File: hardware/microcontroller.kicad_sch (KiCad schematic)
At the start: 12 parts, among them J1 AVR-ISP-6, SW2 SKRPACE010, U1 ATMEGA328P-AU, Y2 Crystal-32kHz

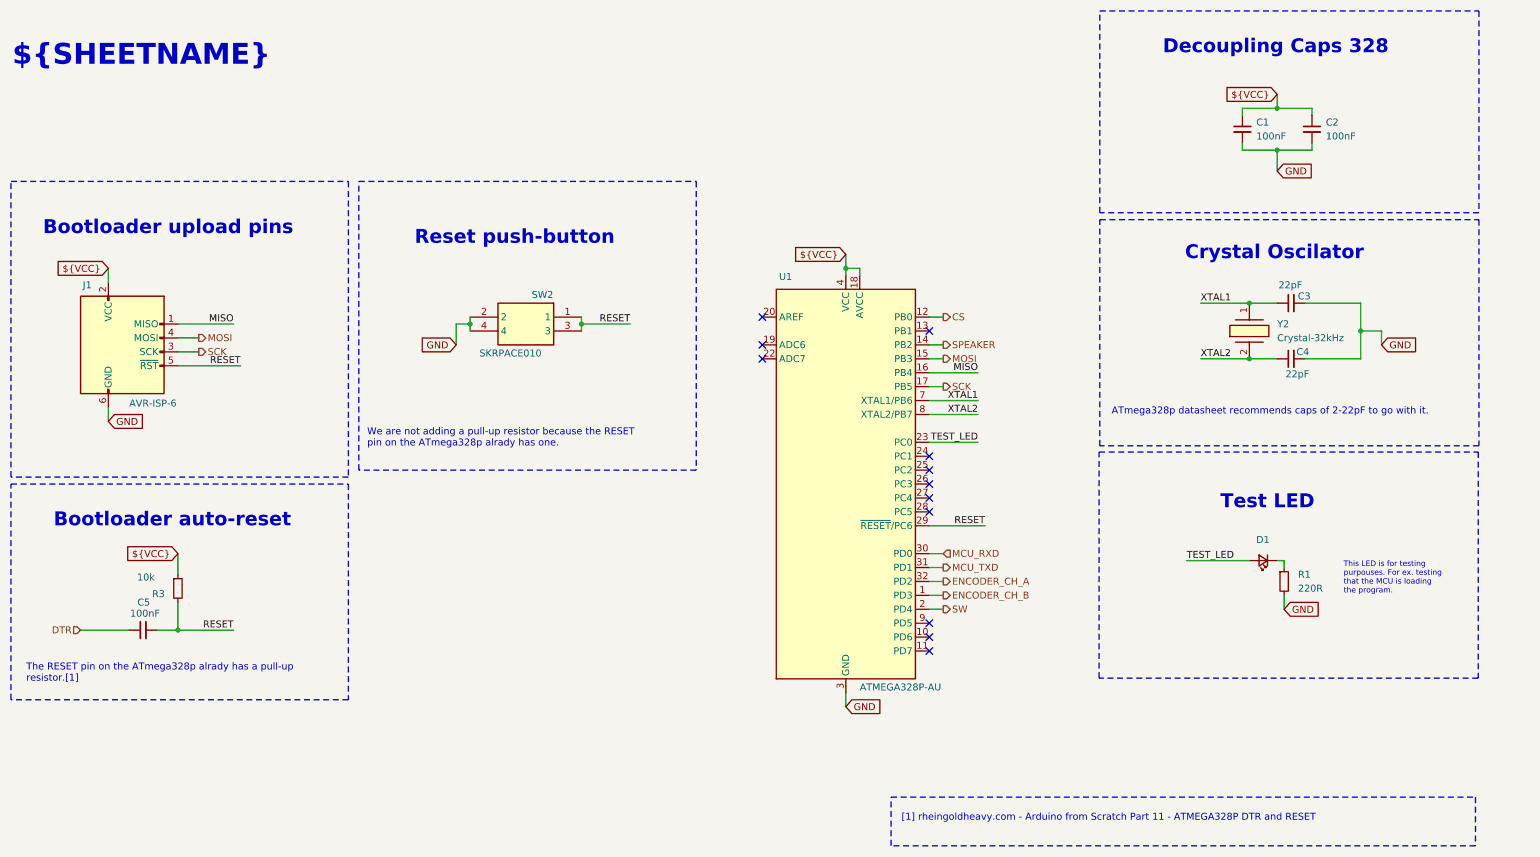
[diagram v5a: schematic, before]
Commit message: Symbols pins vs footprint pins checked
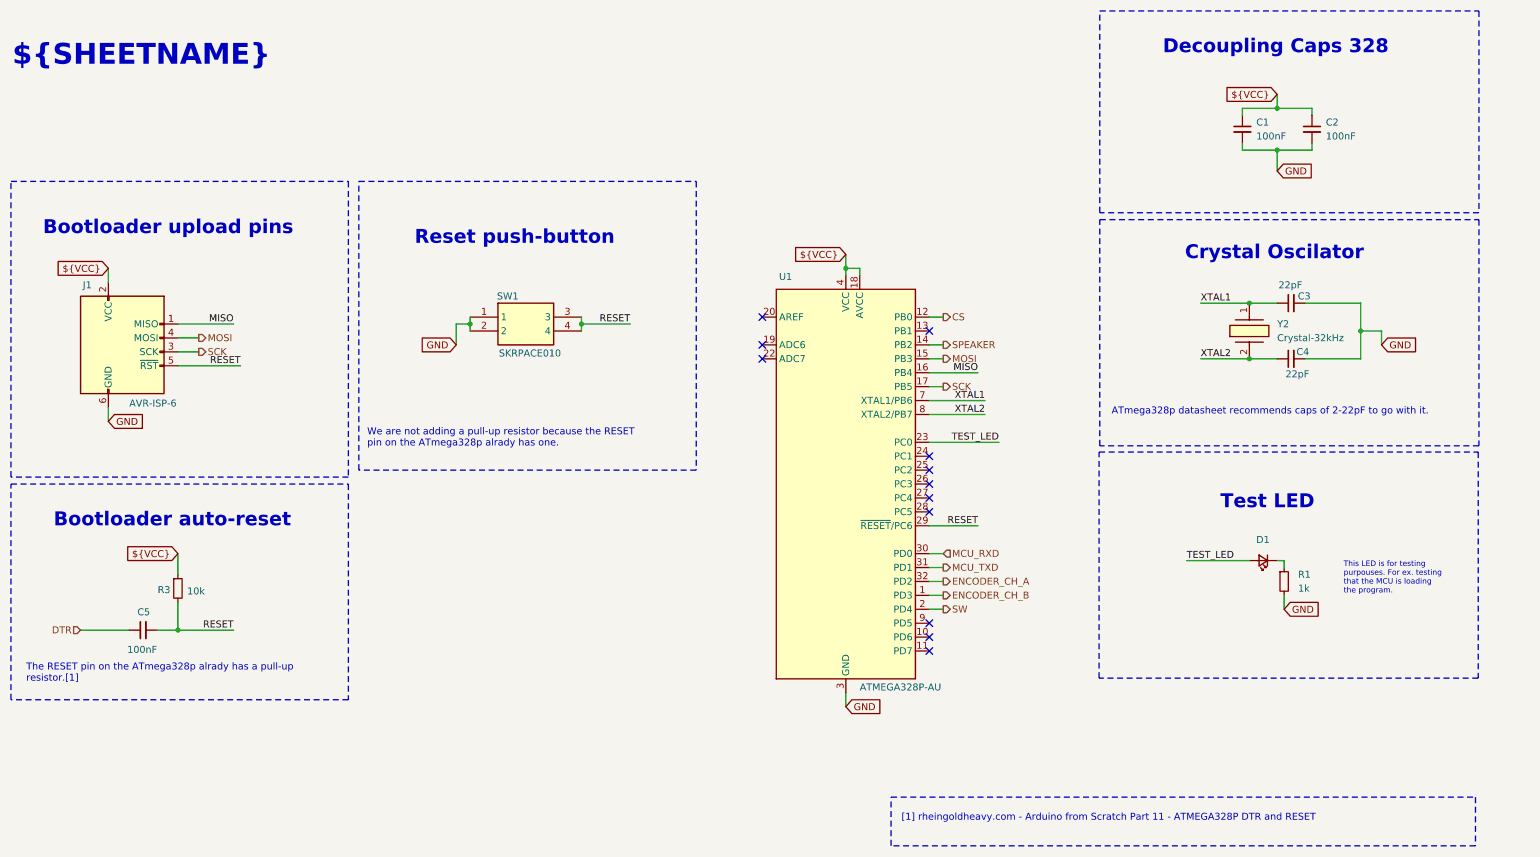
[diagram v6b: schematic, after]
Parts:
- removed SW2: SKRPACE010, kitchen_timer:SW_SKRPACE010, symbol kitchen_timer-symbols_lib:SKRPACE010
- added SW1: SKRPACE010, kitchen_timer:SW_SKRPACE010, symbol kitchen_timer-symbols_lib:SKRPACE010
- R1: value 220R -> 1k; footprint (none) -> Resistor_SMD:R_0805_2012Metric_Pad1.20x1.40mm_HandSolder; Manuf. Name (none) -> UNI-ROYAL(Uniroyal Elec); Manuf. Part # (none) -> 0805W8F1001T5E; Package (none) -> 0805; Supplier Link (none) -> https://jlcpcb.com/partdetail/18201-0805W8F1001T5E/C17513; Supplier Name (none) -> JLCPCB; Supplier Part # (none) -> C17513; Supplier Unit Price (none) -> $0.0017
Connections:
- net GND: now also SW1.1, SW1.2
- net RESET: now also SW1.3, SW1.4

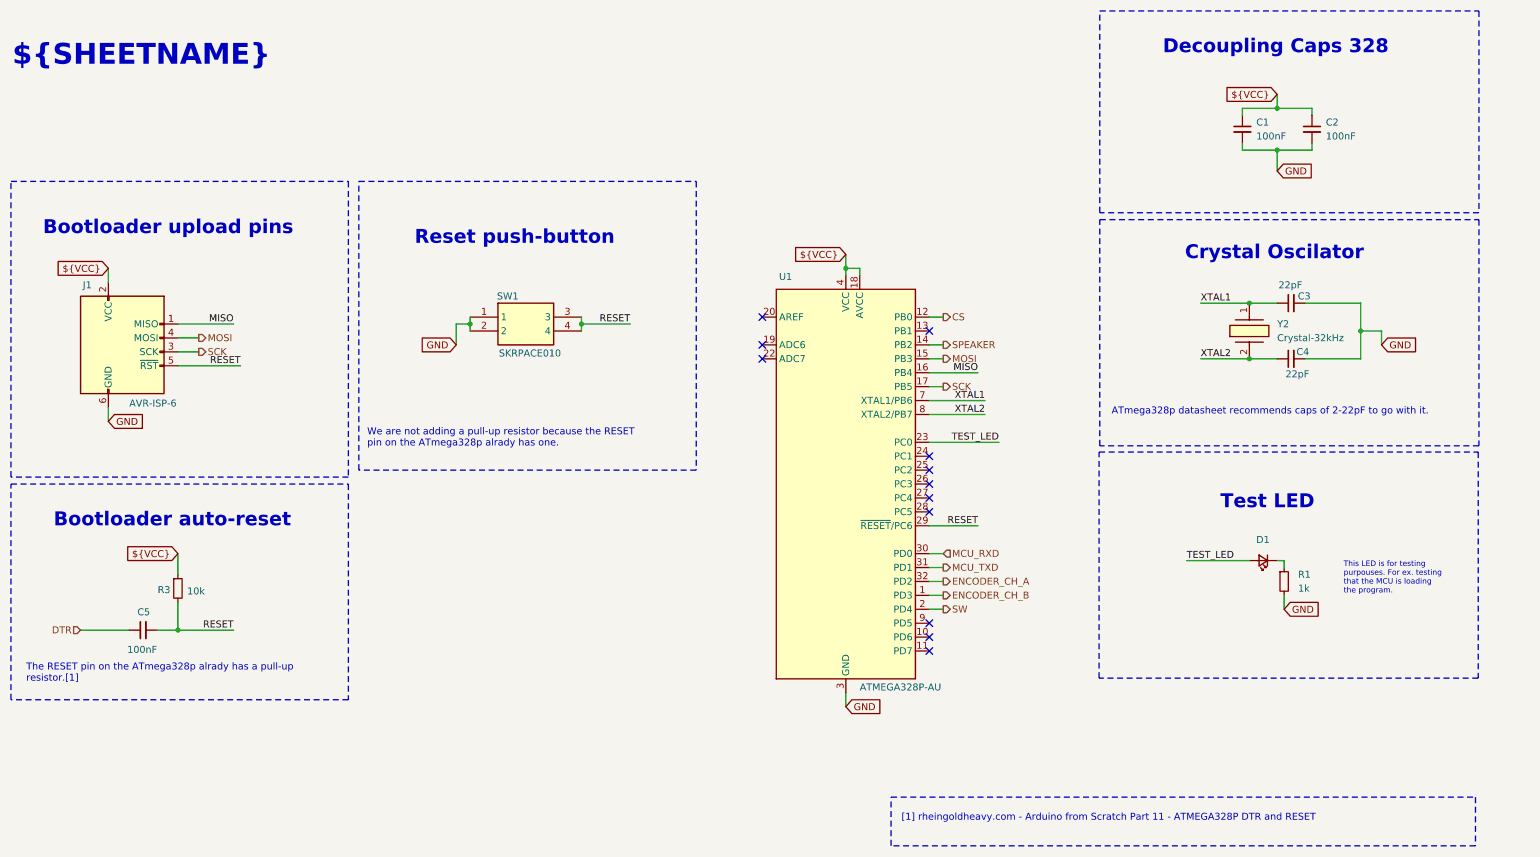
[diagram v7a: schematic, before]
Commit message: Added footprints to mounting holes and selected a part for the test LED.
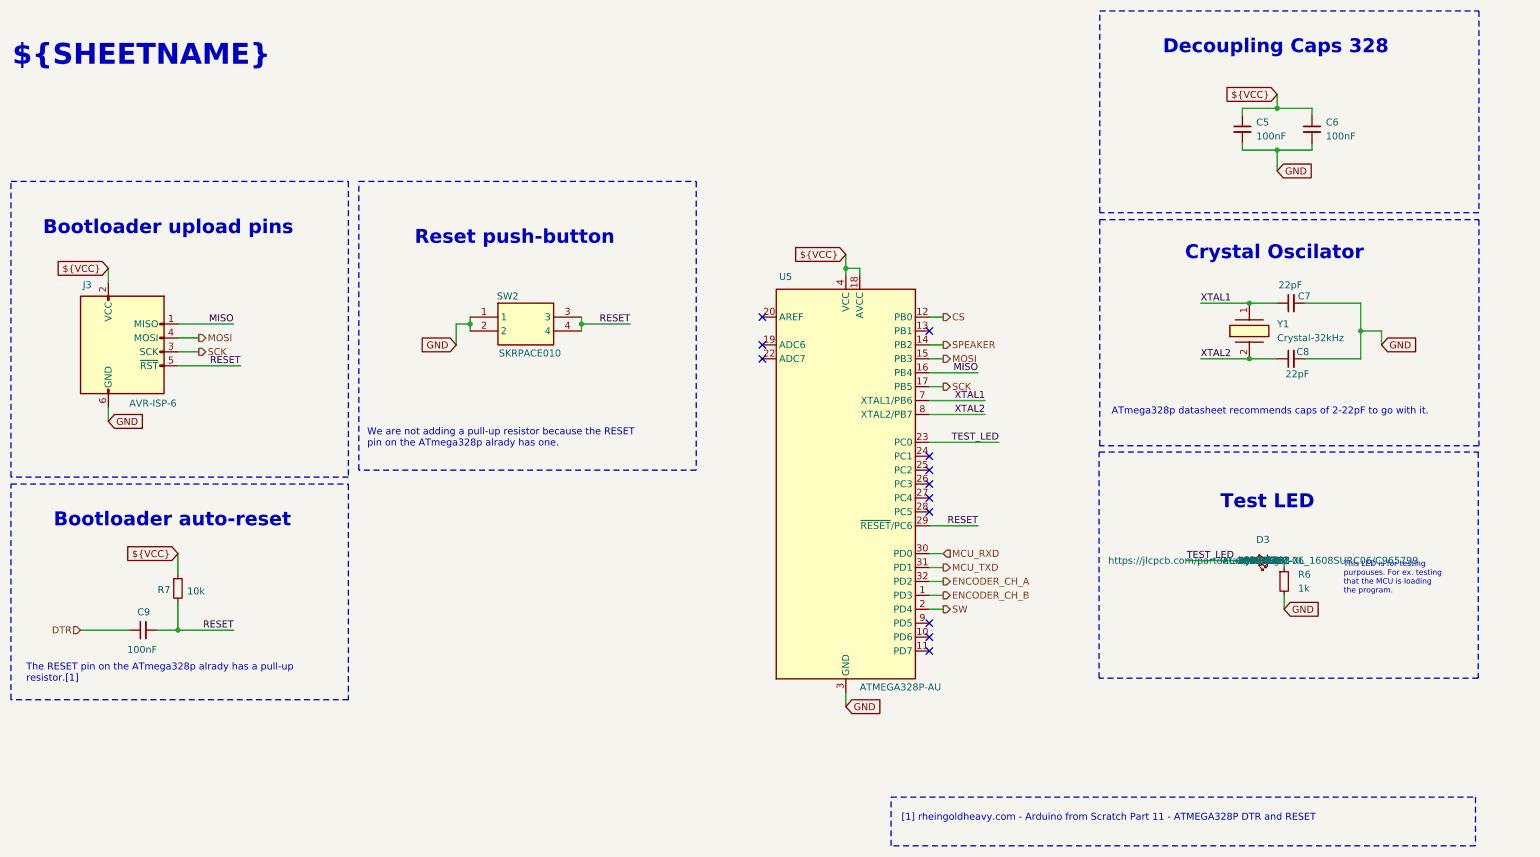
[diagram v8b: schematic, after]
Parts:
- D3: renamed from D1; value LED_Small -> Red test LED; footprint (none) -> LED_SMD:LED_0603_1608Metric_Pad1.05x0.95mm_HandSolder; Manuf. Name (none) -> XINGLIGHT; Manuf. Part # (none) -> XL-1608SURC-06; Package (none) -> 0603_1608; Supplier Link (none) -> https://jlcpcb.com/partdetail/Xinglight-XL_1608SURC06/C9657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; Supplier Name (none) -> JLCPCB; Supplier Part # (none) -> C965799; Supplier Unit Price (none) -> $0.0031
- renumbered C1 to C5, C2 to C6, C3 to C7, C4 to C8, C5 to C9, J1 to J3, R1 to R6, R3 to R7, SW1 to SW2, U1 to U5, Y2 to Y1
